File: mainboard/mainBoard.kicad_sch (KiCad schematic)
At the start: 46 parts, among them J1 XT60PW-M, J2 XT60PW-M, J21 B2B-PH_K, J22 Conn_01x02, J3 XT30PW-M, J4 XT30PW-M, J5 Barrel_Jack, Q1 FQD11P06TM, Q2 FQD11P06TM, U1 TPS565208, U2 TPS565208

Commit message: started work on mainboard
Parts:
- removed J5: Barrel_Jack, Connector_BarrelJack:BarrelJack_Kycon_KLDX-0202-xC_Horizontal, symbol Connector:Barrel_Jack
- removed L1: 3.3uH, Inductor_SMD:L_Abracon_ASPI-0630LR, symbol Device:L
- removed L2: 2.2uH, Inductor_SMD:L_Abracon_ASPI-0630LR, symbol Device:L
- added C17, C18, C19, C7: 10uF, Capacitor_SMD:C_0805_2012Metric_Pad1.18x1.45mm_HandSolder, symbol Device:C
- added C20, C21: 0.1uF, Capacitor_SMD:C_0805_2012Metric_Pad1.18x1.45mm_HandSolder, symbol Device:C
- added C22, C23: 22uF, Capacitor_SMD:C_0805_2012Metric_Pad1.18x1.45mm_HandSolder, symbol Device:C
- added D4: LED, Diode_SMD:D_0805_2012Metric_Pad1.15x1.40mm_HandSolder, symbol Device:LED
- added L1, L5: 3.3uH, Inductor_SMD:L_Abracon_ASPI-0630LR, symbol Device:L_Ferrite
- added L3: 2.2uH, Inductor_SMD:L_Abracon_ASPI-0630LR, symbol Device:L_Ferrite
- added Q3: FQD11P06TM, Package_TO_SOT_SMD:TO-252-2, symbol FQD11P06TM:FQD11P06TM
- added R23: 0, Resistor_SMD:R_1210_3225Metric_Pad1.30x2.65mm_HandSolder, symbol Device:R_US
- added R27: 100, Resistor_SMD:R_0805_2012Metric_Pad1.20x1.40mm_HandSolder, symbol Device:R_US
- added R28, R29: 10K, Resistor_SMD:R_0805_2012Metric_Pad1.20x1.40mm_HandSolder, symbol Device:R_US
- added R30: 87370, Resistor_SMD:R_0805_2012Metric_Pad1.20x1.40mm_HandSolder, symbol Device:R_US
- added R31: 1K, Resistor_SMD:R_0805_2012Metric_Pad1.20x1.40mm_HandSolder, symbol Device:R_US
- added U3: TPS565208, Package_TO_SOT_SMD:SOT-23-6, symbol Regulator_Switching:TPS565208
- R4: value 150 -> 500
- R8: value 68 -> 300
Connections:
- net +12V: now also J1.2 (Pin_2), J2.2 (Pin_2), C17.1, C18.1, Q3.3 (D), R23.2, R28.1; no longer J1.1 (Pin_1), J2.1 (Pin_1)
- net +3V3: now also J4.2 (Pin_2), L3.2; no longer J4.1 (Pin_1)
- net +5V: now also J3.2 (Pin_2), L1.2; no longer J3.1 (Pin_1)
- net GND: now also J1.1 (Pin_1), J2.1 (Pin_1), J3.1 (Pin_1), J4.1 (Pin_1), C17.2, C18.2, C19.2, C20.2, C22.2, C23.2, C7.2, D4.1 (K), R27.2, R29.1, U3.1 (GND); no longer J1.2 (Pin_2), J2.2 (Pin_2), J3.2 (Pin_2), J4.2 (Pin_2)
- net at C11.2, U2.2 (SW): now also L3.1
- net at C4.2, U1.2 (SW): now also L1.1
- new net: C19.1, C20.1, C7.1, Q3.2 (S), R23.1, U3.3 (VIN)
- new net: C21.1, U3.6 (VBST)
- new net: C21.2, L5.1, U3.2 (SW)
- new net: R29.2, R30.1, U3.4 (VFB)
- new net: R28.2, U3.5 (EN)
- new net: Q3.1 (G), R27.1
- new net: D4.2 (A), R31.2
- new net +7.5V: C22.1, C23.1, L5.2, R30.2, R31.1
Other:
- note added: "12V to 7.4V, 5A"
- note removed: "Jetson Power"
- note removed: "cursed barrel jack to barrel jack"
- moved on the sheet: C1, C10, C11, C12, C13, C2, C3, C4, C5, C6, C8, C9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

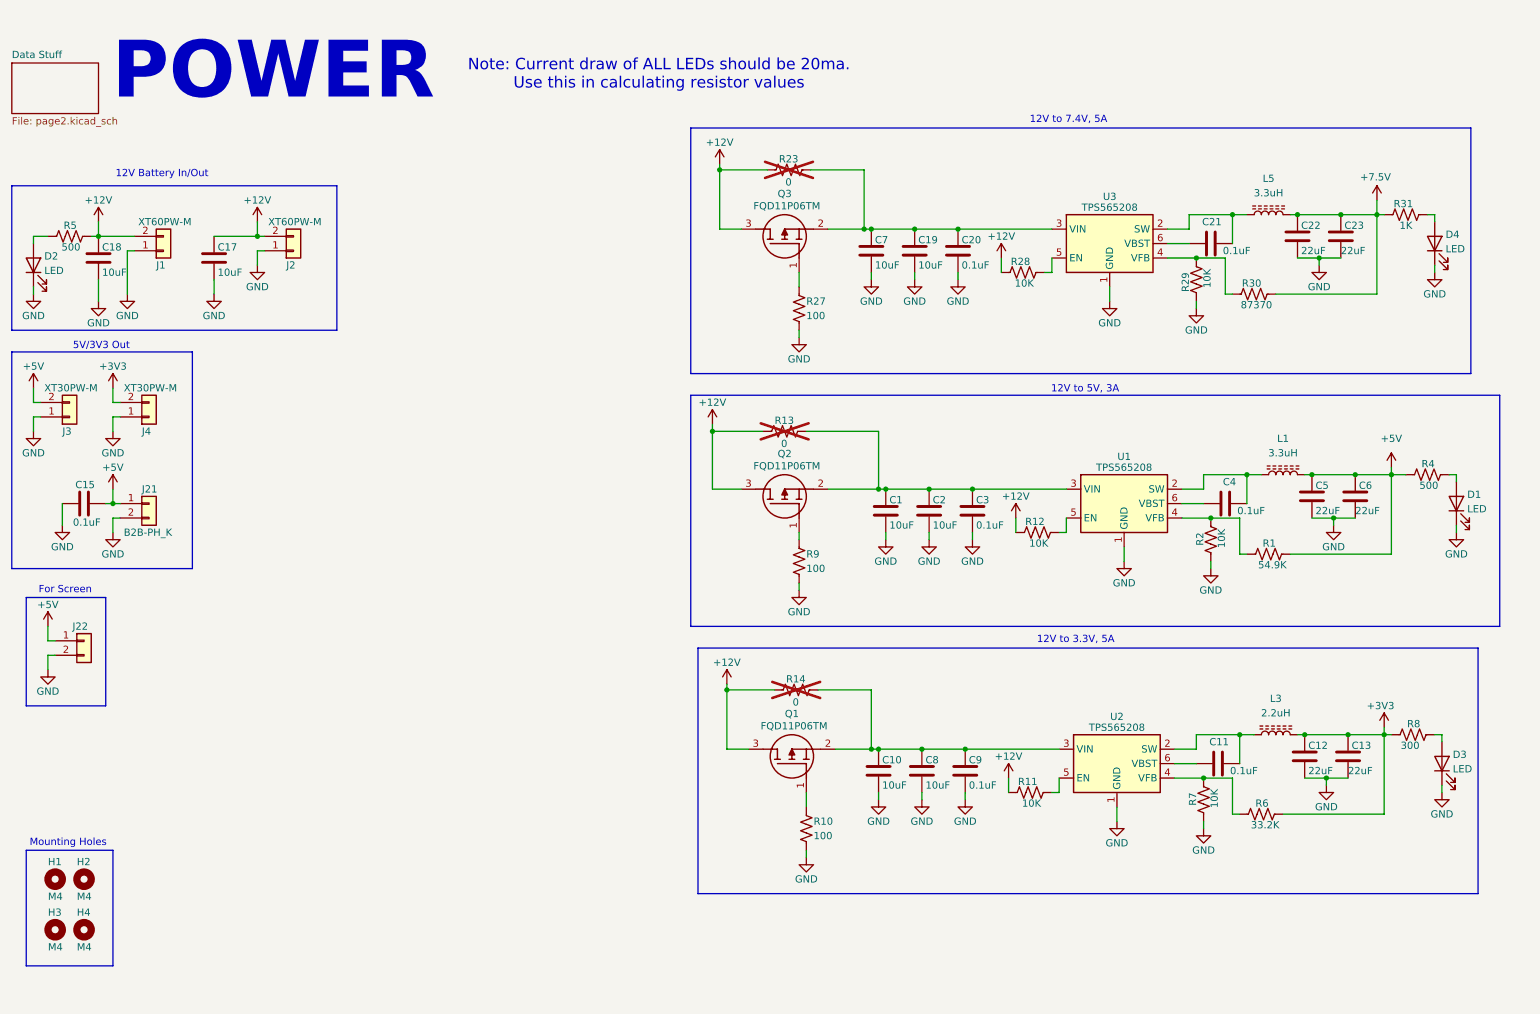
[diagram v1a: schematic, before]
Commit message: layed out PCB, started routing of mainboard
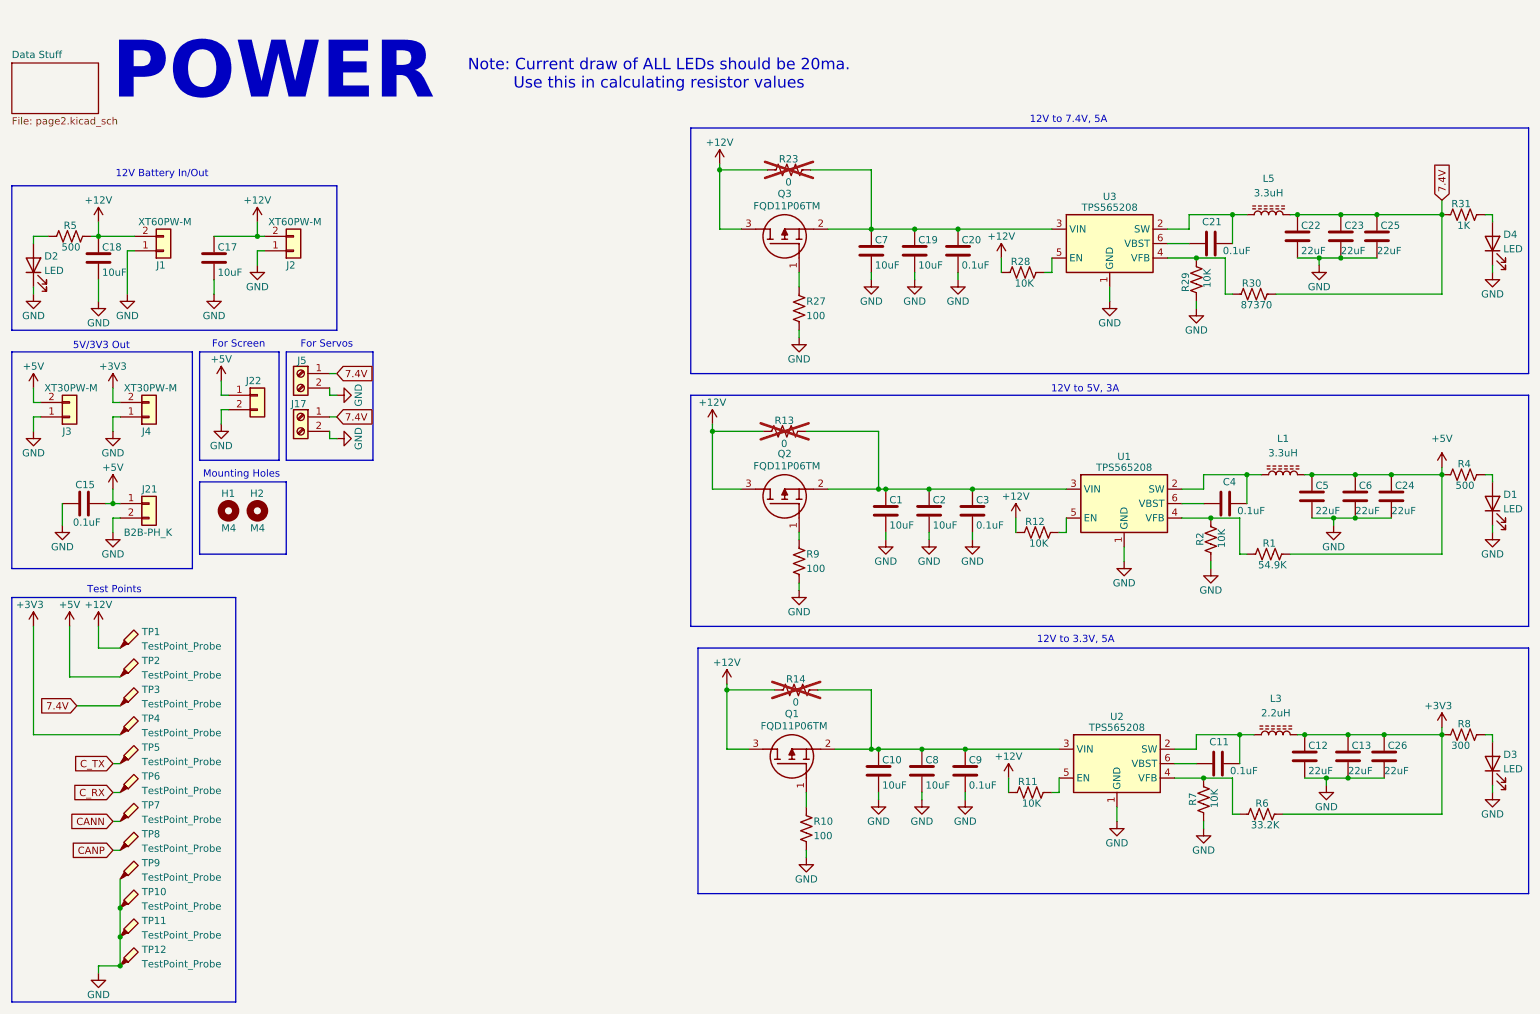
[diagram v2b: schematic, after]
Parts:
- removed H3, H4: M4, MountingHole:MountingHole_4.3mm_M4_DIN965, symbol Mechanical:MountingHole
- added C24, C25, C26: 22uF, Capacitor_SMD:C_0805_2012Metric_Pad1.18x1.45mm_HandSolder, symbol Device:C
- added J17, J5: 2 pin screw, TerminalBlock_Phoenix:TerminalBlock_Phoenix_MKDS-1,5-2_1x02_P5.00mm_Horizontal, symbol Connector:Screw_Terminal_01x02
- added TP1, TP10, TP11, TP12, TP2, TP3, TP4, TP5, TP6, TP7, TP8, TP9: TestPoint_Probe, TestPoint:TestPoint_Pad_D2.0mm, symbol Connector:TestPoint_Probe
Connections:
- net +12V: now also TP1.1
- net +3V3: now also C26.1, TP4.1
- net +5V: now also C24.1, TP2.1
- net GND: now also C24.2, C25.2, C26.2, J17.2 (Pin_2), J5.2 (Pin_2), TP10.1, TP11.1, TP12.1, TP9.1
- net +7.5V renamed 7.4V
- net 7.4V: now also C25.1, J17.1 (Pin_1), J5.1 (Pin_1), TP3.1
- new net CANN: TP7.1
- new net CANP: TP8.1
- new net C_RX: TP6.1
- new net C_TX: TP5.1
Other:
- note added: "For Servos"
- note added: "Test Points"
- moved on the sheet: D1, D3, D4, H1, H2, J22, R31, R4, R8

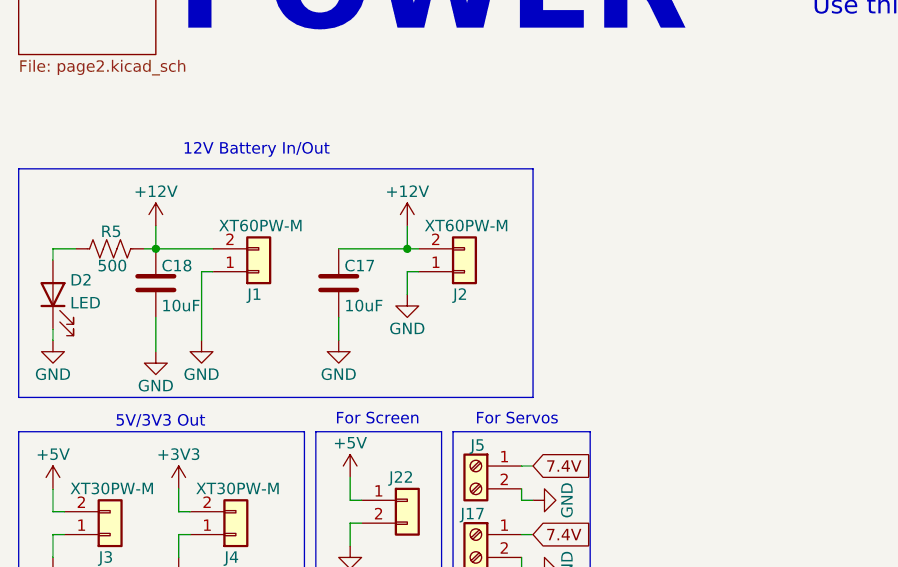
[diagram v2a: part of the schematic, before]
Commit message: added some capacitors
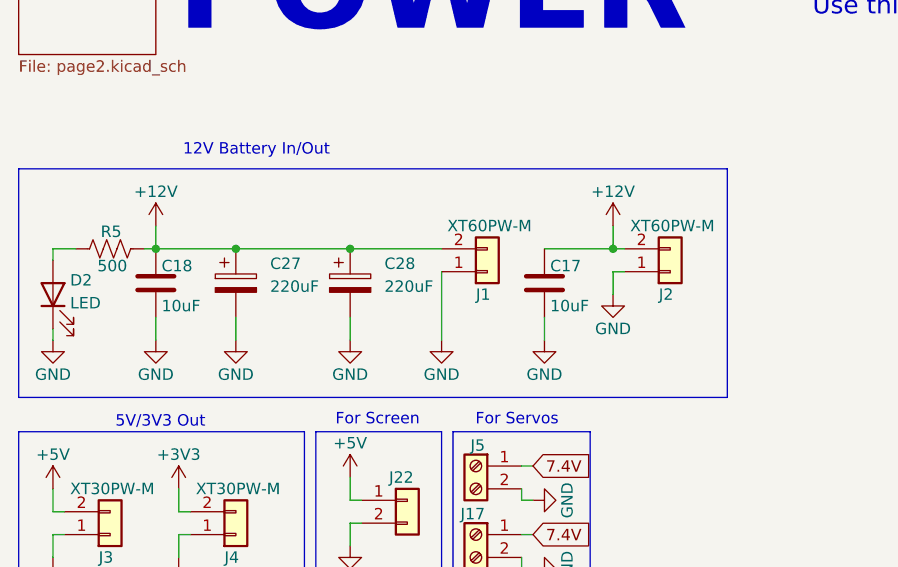
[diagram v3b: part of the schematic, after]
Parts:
- added C27, C28: 220uF, Capacitor_THT:CP_Radial_D6.3mm_P2.50mm, symbol Device:C_Polarized
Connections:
- net +12V: now also C27.1, C28.1
- net GND: now also C27.2, C28.2
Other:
- moved on the sheet: C17, J1, J2
